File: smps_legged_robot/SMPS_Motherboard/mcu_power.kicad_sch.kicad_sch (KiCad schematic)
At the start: 26 parts, among them J10 FTSH-107-01-F-DV-K-P-TR, SW2 MJTP1140ATR, SW3 SW_SPDT, U1 STM32H750VBTx, U1 W25Q128JVS, Y1 ABM10W-48.0000MHZ-8-D7G-T3

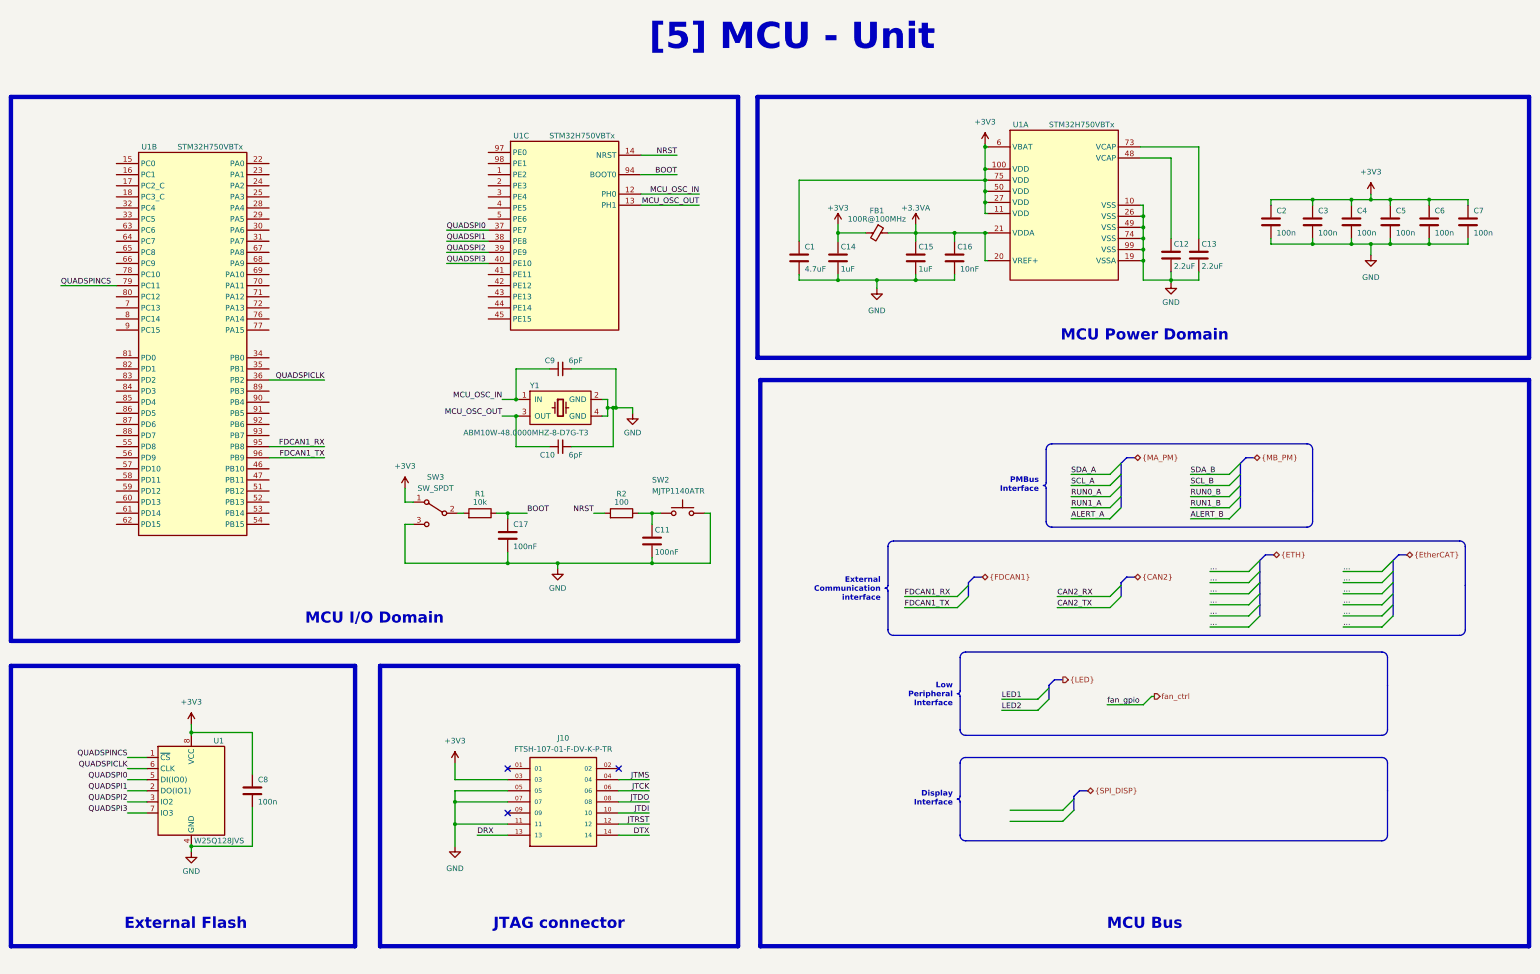
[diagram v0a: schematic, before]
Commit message: Buck module finished pending review
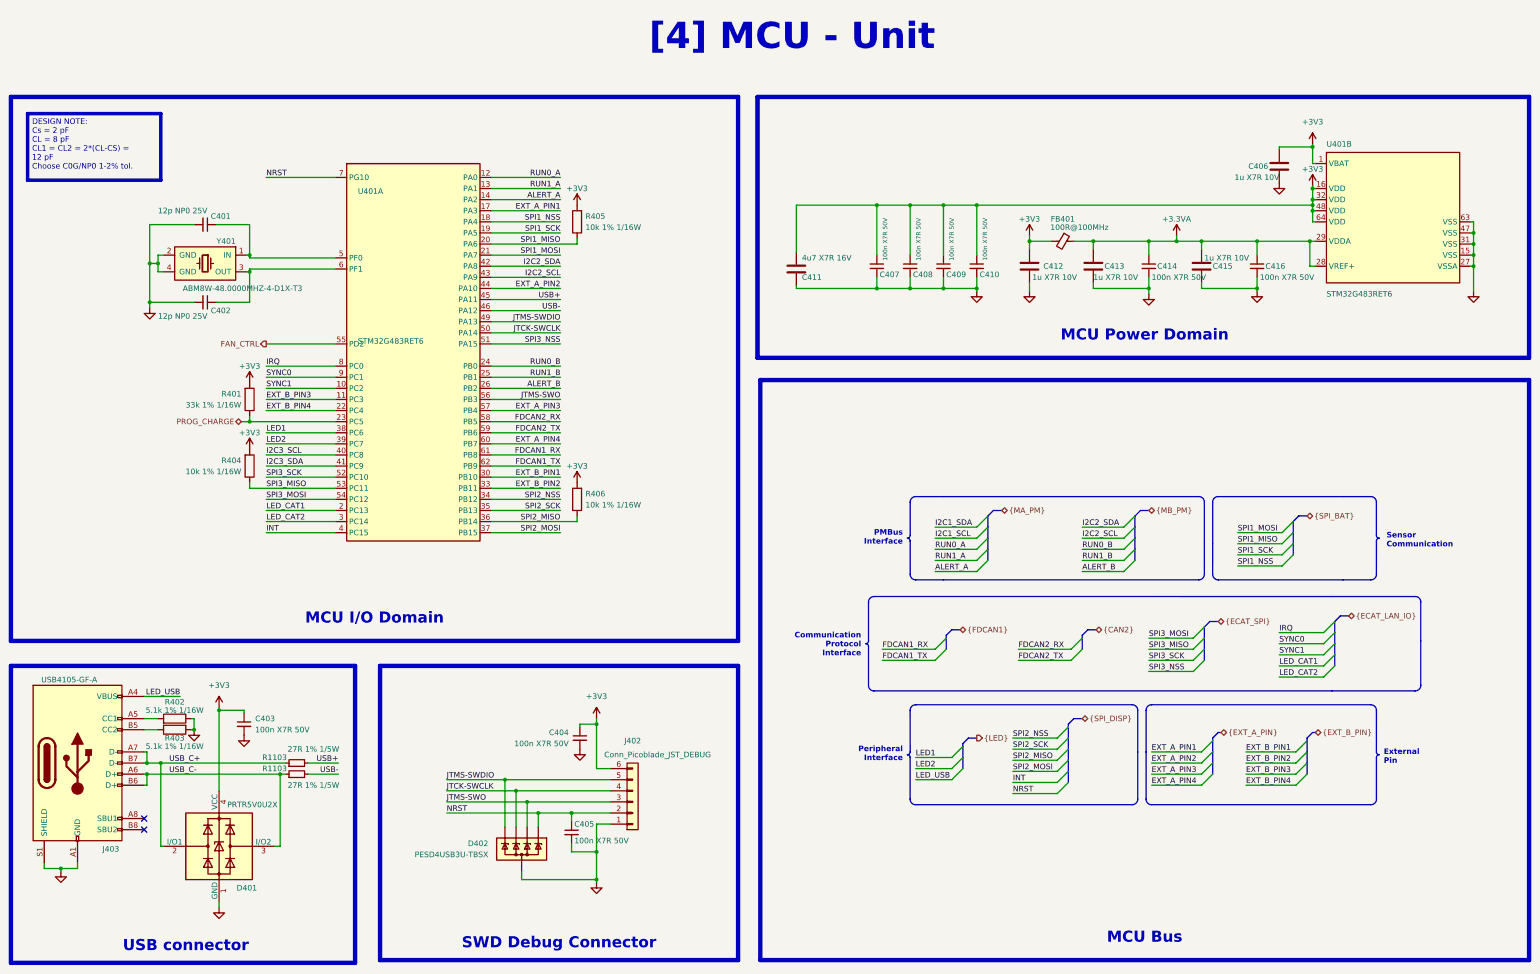
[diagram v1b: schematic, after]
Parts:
- removed C1: 4.7uF, symbol Device:C
- removed C11, C17: 100nF, symbol Device:C
- removed C12, C13: 2.2uF, symbol Device:C
- removed C14, C15: 1uF, symbol Device:C
- removed C16: 10nF, symbol Device:C
- removed C2, C3, C4, C5, C6, C7, C8: 100n, symbol Device:C
- removed J10: FTSH-107-01-F-DV-K-P-TR, FTSH-107-01-F-DV-K-P-TR:SAMTEC_FTSH-107-01-F-DV-K-P-TR, symbol FTSH-107-01-F-DV-K-P-TR:FTSH-107-01-F-DV-K-P-TR
- removed R1: 10k, symbol Device:R
- removed R2: 100, symbol Device:R
- removed SW2: MJTP1140ATR, 0_switch_button:MJTP1140ATR, symbol Switch:SW_Push
- removed SW3: SW_SPDT, symbol Switch:SW_SPDT
- removed U1: STM32H750VBTx, Package_QFP:LQFP-100_14x14mm_P0.5mm, symbol MCU_ST_STM32H7:STM32H730VBTx
- added C403, C404, C405, C407, C408, C409, C410, C414, C416: 100n X7R 50V, 0_capacitor_smd:C_0402_1005_DensityHigh, symbol Device:C_Small
- added C406, C412, C413, C415: 1u X7R 10V, 0_capacitor_smd:C_0402_1005_DensityHigh, symbol Device:C
- added C411: 4u7 X7R 16V, 0_capacitor_smd:C_0603_1608_DensityHigh, symbol Device:C
- added D401: PRTR5V0U2X, Package_TO_SOT_SMD:SOT-143, symbol Power_Protection:PRTR5V0U2X
- added D402: PESD4USB3U-TBSX, 0_package_DFN_QFN:SOT1176D, symbol 0_power_protection:PESD4USB3U-TBSX
- added J402: Conn_Picoblade_JST_DEBUG, 0_connectors:CONN_SM06B-GHS-TB_JST, symbol Connector_Generic:Conn_01x06
- added J403: USB4105-GF-A, Connector_USB:USB_C_Receptacle_GCT_USB4105-xx-A_16P_TopMnt_Horizontal, symbol Connector:USB_C_Receptacle_USB2.0
- added R1103 (x2): 27R 1% 1/5W, 0_resistor_smd:R_0402_1005_DensityHigh, symbol Device:R_Small
- added R401: 33k 1% 1/16W, 0_resistor_smd:R_0402_1005_DensityHigh, symbol Device:R
- added R402, R403: 5.1k 1% 1/16W, 0_resistor_smd:R_0402_1005_DensityHigh, symbol Device:R
- added R404, R405, R406: 10k 1% 1/16W, 0_resistor_smd:R_0402_1005_DensityHigh, symbol Device:R
- added U401: STM32G483RET6, Package_QFP:LQFP-64_10x10mm_P0.5mm, symbol MCU_ST_STM32G4:STM32G483RETx
- C401: renamed from C9; value 6pF -> 12p NP0 25V
- C402: renamed from C10; value 6pF -> 12p NP0 25V
- Y401: renamed from Y1; value ABM10W-48.0000MHZ-8-D7G-T3 -> ABM8W-48.0000MHZ-4-D1X-T3; footprint Crystal:Crystal_SMD_Abracon_ABM10-4Pin_2.5x2.0mm -> 0_diode_smd:ABM8W480000MHZ6D1XT3
- renumbered FB1 to FB401
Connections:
- net +3.3VA: now also C413.1, C414.1, C415.1, C416.1, U401.28 (VREF+), U401.29 (VDDA)
- net +3V3: now also C403.1, C404.1, C406.1, C407.1, C408.1, C409.1, C410.1, C411.1, C412.1, D401.4 (VCC), J402.6 (Pin_6), R401.2, R404.2, R405.2, R406.2, U401.1 (VBAT), U401.16 (VDD), U401.32 (VDD), U401.48 (VDD), U401.64 (VDD)
- net ALERT_A: now also U401.14 (PA2)
- net ALERT_B: now also U401.26 (PB2)
- net FDCAN1_RX: now also U401.61 (PB8)
- net FDCAN1_TX: now also U401.62 (PB9)
- net GND: now also C403.2, C404.2, C405.2, C406.2, C407.2, C408.2, C409.2, C410.2, C411.2, C412.2, C413.2, C414.2, C415.2, C416.2, D401.1 (GND), D402.3 (A), D402.8 (A), J402.1 (Pin_1), J403.A1 (GND), J403.A12 (GND), J403.B1 (GND), J403.B12 (GND), J403.S1 (SHIELD), R402.1, R403.2, U401.15 (VSS), U401.27 (VSSA), U401.31 (VSS), U401.47 (VSS), U401.63 (VSS)
- net LED1: now also U401.38 (PC6)
- net LED2: now also U401.39 (PC7)
- net NRST: now also C405.1, D402.1 (K), D402.10 (K), J402.2 (Pin_2), U401.7 (PG10)
- net RUN0_A: now also U401.12 (PA0)
- net RUN0_B: now also U401.24 (PB0)
- net RUN1_A: now also U401.13 (PA1)
- net RUN1_B: now also U401.25 (PB1)
- net MCU_OSC_IN: no longer names the net of C401.1, Y401.1 (IN)
- net MCU_OSC_IN: now also U401.5 (PF0)
- net MCU_OSC_OUT: no longer names the net of C402.1, Y401.3 (OUT)
- net MCU_OSC_OUT: now also U401.6 (PF1)
- new net: J403.B5 (CC2), R403.1
- new net: J403.A5 (CC1), R402.2
- new net EXT_A_PIN1: U401.17 (PA3)
- new net EXT_A_PIN2: U401.44 (PA10)
- new net EXT_A_PIN3: U401.57 (PB4)
- new net EXT_A_PIN4: U401.60 (PB7)
- new net EXT_B_PIN1: U401.30 (PB10)
- new net EXT_B_PIN2: U401.33 (PB11)
- new net EXT_B_PIN3: U401.11 (PC3)
- new net EXT_B_PIN4: U401.22 (PC4)
- new net FAN_CTRL: U401.55 (PD2)
- new net FDCAN2_RX: U401.58 (PB5)
- new net FDCAN2_TX: U401.59 (PB6)
- new net I2C2_SCL: U401.43 (PA9)
- new net I2C2_SDA: U401.42 (PA8)
- new net I2C3_SCL: U401.40 (PC8)
- new net I2C3_SDA: U401.41 (PC9)
- new net INT: U401.4 (PC15)
- new net IRQ: U401.8 (PC0)
- new net JTCK-SWCLK: D402.4 (K), D402.7 (K), J402.4 (Pin_4), U401.50 (PA14)
- new net JTMS-SWDIO: D402.5 (K), D402.6 (K), J402.5 (Pin_5), U401.49 (PA13)
- new net JTMS-SWO: D402.2 (K), D402.9 (K), J402.3 (Pin_3), U401.56 (PB3)
- new net LED_CAT1: U401.2 (PC13)
- new net LED_CAT2: U401.3 (PC14)
- new net LED_USB: J403.A4 (VBUS), J403.A9 (VBUS), J403.B4 (VBUS), J403.B9 (VBUS)
- new net PROG_CHARGE: R401.1, U401.23 (PC5)
- new net SPI1_MISO: R405.1, U401.20 (PA6)
- new net SPI1_MOSI: U401.21 (PA7)
- new net SPI1_NSS: U401.18 (PA4)
- new net SPI1_SCK: U401.19 (PA5)
- new net SPI2_MISO: R406.1, U401.36 (PB14)
- new net SPI2_MOSI: U401.37 (PB15)
- new net SPI2_NSS: U401.34 (PB12)
- new net SPI2_SCK: U401.35 (PB13)
- new net SPI3_MISO: R404.1, U401.53 (PC11)
- new net SPI3_MOSI: U401.54 (PC12)
- new net SPI3_NSS: U401.51 (PA15)
- new net SPI3_SCK: U401.52 (PC10)
- new net SYNC0: U401.9 (PC1)
- new net SYNC1: U401.10 (PC2)
- new net USB+: R1103.2, U401.45 (PA11)
- new net USB-: R1103.2, U401.46 (PA12)
- new net USB_C+: D401.2 (I/O1), J403.A7 (D-), J403.B7 (D-), R1103.1
- new net USB_C-: D401.3 (I/O2), J403.A6 (D+), J403.B6 (D+), R1103.1
- no-connect marks 3 -> 2
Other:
- moved on the sheet: C401, C402, FB401, Y401

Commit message: Rev 1.0 of smps finished -> waiting for verification
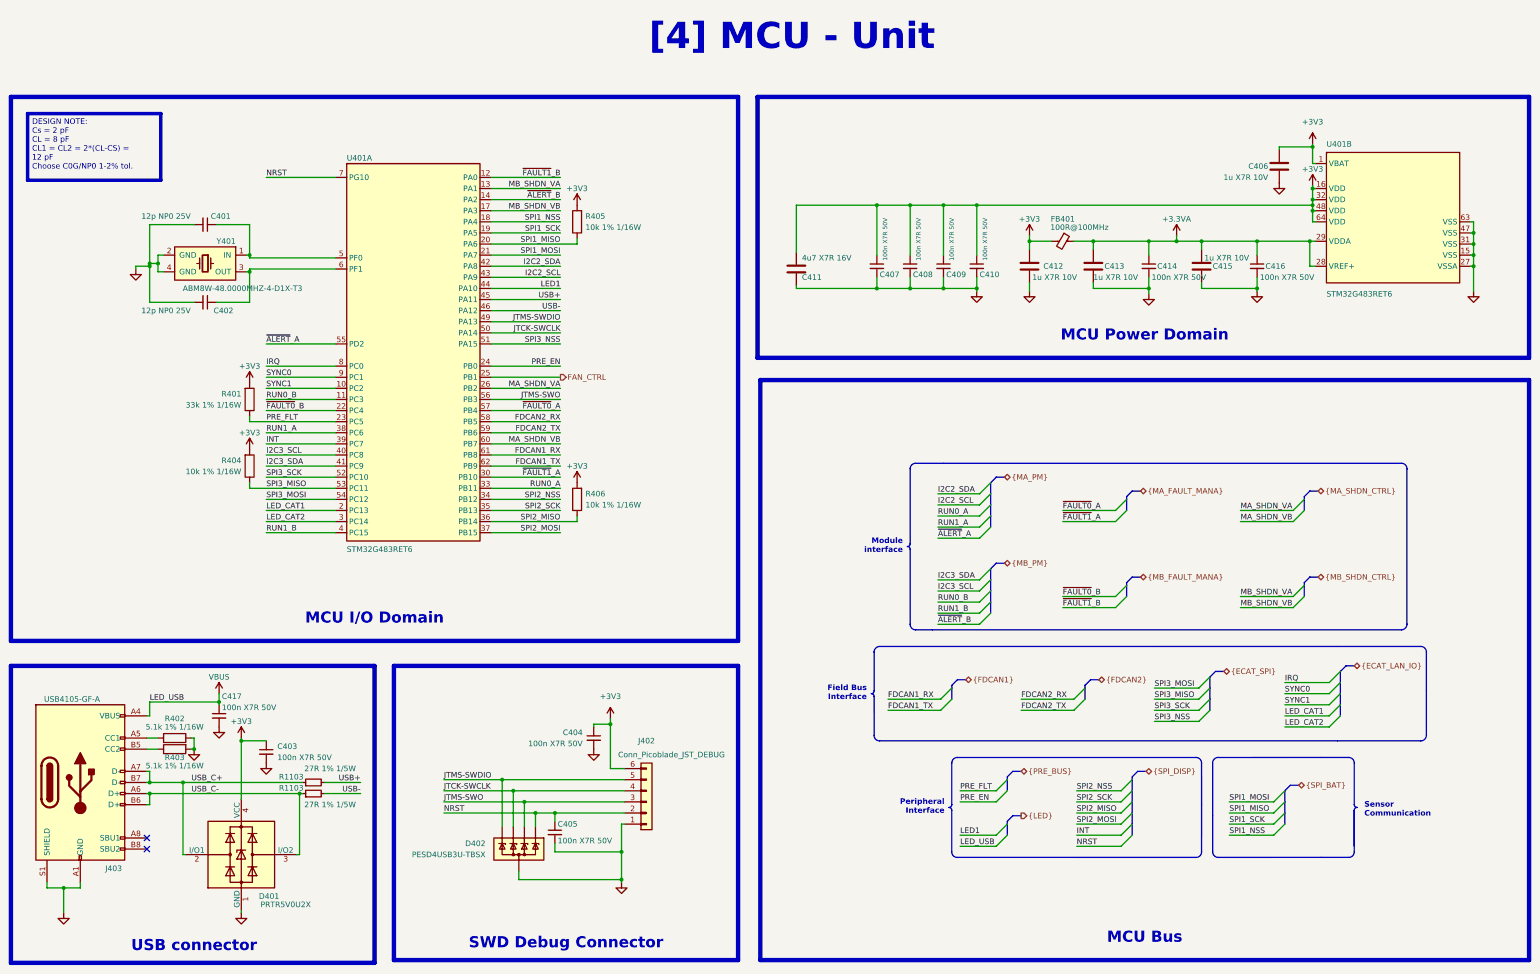
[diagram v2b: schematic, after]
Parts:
- added C417: 100n X7R 50V, 0_capacitor_smd:C_0402_1005_DensityHigh, symbol Device:C_Small
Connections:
- net EXT_A_PIN2 is gone; now on net LED1: U401.44 (PA10)
- net EXT_B_PIN2 is gone; now on net RUN0_A: U401.33 (PB11)
- net EXT_B_PIN3 is gone; now on net RUN0_B: U401.11 (PC3)
- net LED2 is gone; now on net INT: U401.39 (PC7)
- net FAN_CTRL: now also U401.25 (PB1); no longer U401.55 (PD2)
- net GND: now also C417.2
- net INT: no longer U401.4 (PC15)
- net LED1: no longer U401.38 (PC6)
- net RUN0_A: no longer U401.12 (PA0)
- net RUN0_B: no longer U401.24 (PB0)
- net RUN1_A: now also U401.38 (PC6); no longer U401.13 (PA1)
- net RUN1_B: now also U401.4 (PC15); no longer U401.25 (PB1)
- net ALERT_A renamed ~{ALERT}_B
- net ALERT_B renamed MA_SHDN_VA
- net EXT_A_PIN1 renamed MB_SHDN_VB
- net EXT_A_PIN3 renamed ~{FAULT0}_A
- net EXT_A_PIN4 renamed MA_SHDN_VB
- net EXT_B_PIN1 renamed ~{FAULT1}_A
- net EXT_B_PIN4 renamed ~{FAULT0}_B
- net LED_USB renamed VBUS
- net VBUS: now also C417.1
- net PROG_CHARGE renamed PRE_FLT
- new net MB_SHDN_VA: U401.13 (PA1)
- new net PRE_EN: U401.24 (PB0)
- new net ~{ALERT}_A: U401.55 (PD2)
- new net ~{FAULT1}_B: U401.12 (PA0)
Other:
- moved on the sheet: C403, C404, C405, D401, D402, J402, J403, R1103, R402, R403

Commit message: Geode test board ready to order
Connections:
- net LED1 is gone; now on net RUN1_A: U401.44 (PA10)
- net +3V3: no longer C403.1, D401.4 (VCC)
- net RUN0_A: now also U401.38 (PC6); no longer U401.33 (PB11)
- net RUN1_A: no longer U401.38 (PC6)
- net VBUS: now also C403.1, D401.4 (VCC)
- net CC2: now reaches J403.B5 (CC2), R403.1
- net CLOCK_IN: now reaches C401.1, U401.5 (PF0), Y401.1 (IN)
- net CLOCK_OUT: now reaches C402.1, U401.6 (PF1), Y401.3 (OUT)
- net CC1: now reaches J403.A5 (CC1), R402.2
- new net TEMP_SENS: U401.33 (PB11)
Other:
- moved on the sheet: C403, C417, R402, R403
